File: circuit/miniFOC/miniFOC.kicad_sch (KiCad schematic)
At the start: 79 parts, among them J1 Conn_01x05, J2 Conn_01x03, J3 Conn_01x04, J4 Conn_01x02, J5 Conn_01x01, J6 Conn_01x01, J7 Conn_01x01, Q1 RU30J30M, Q2 RU30J30M, Q3 RU30J30M, U1 XC6206P332MR, U2 CH32V203C8T6, U3 LM321, U4 COS722MR, U5 BDR2L00, U6 BDR2L00, U7 BDR2L00, U8 JW5017S

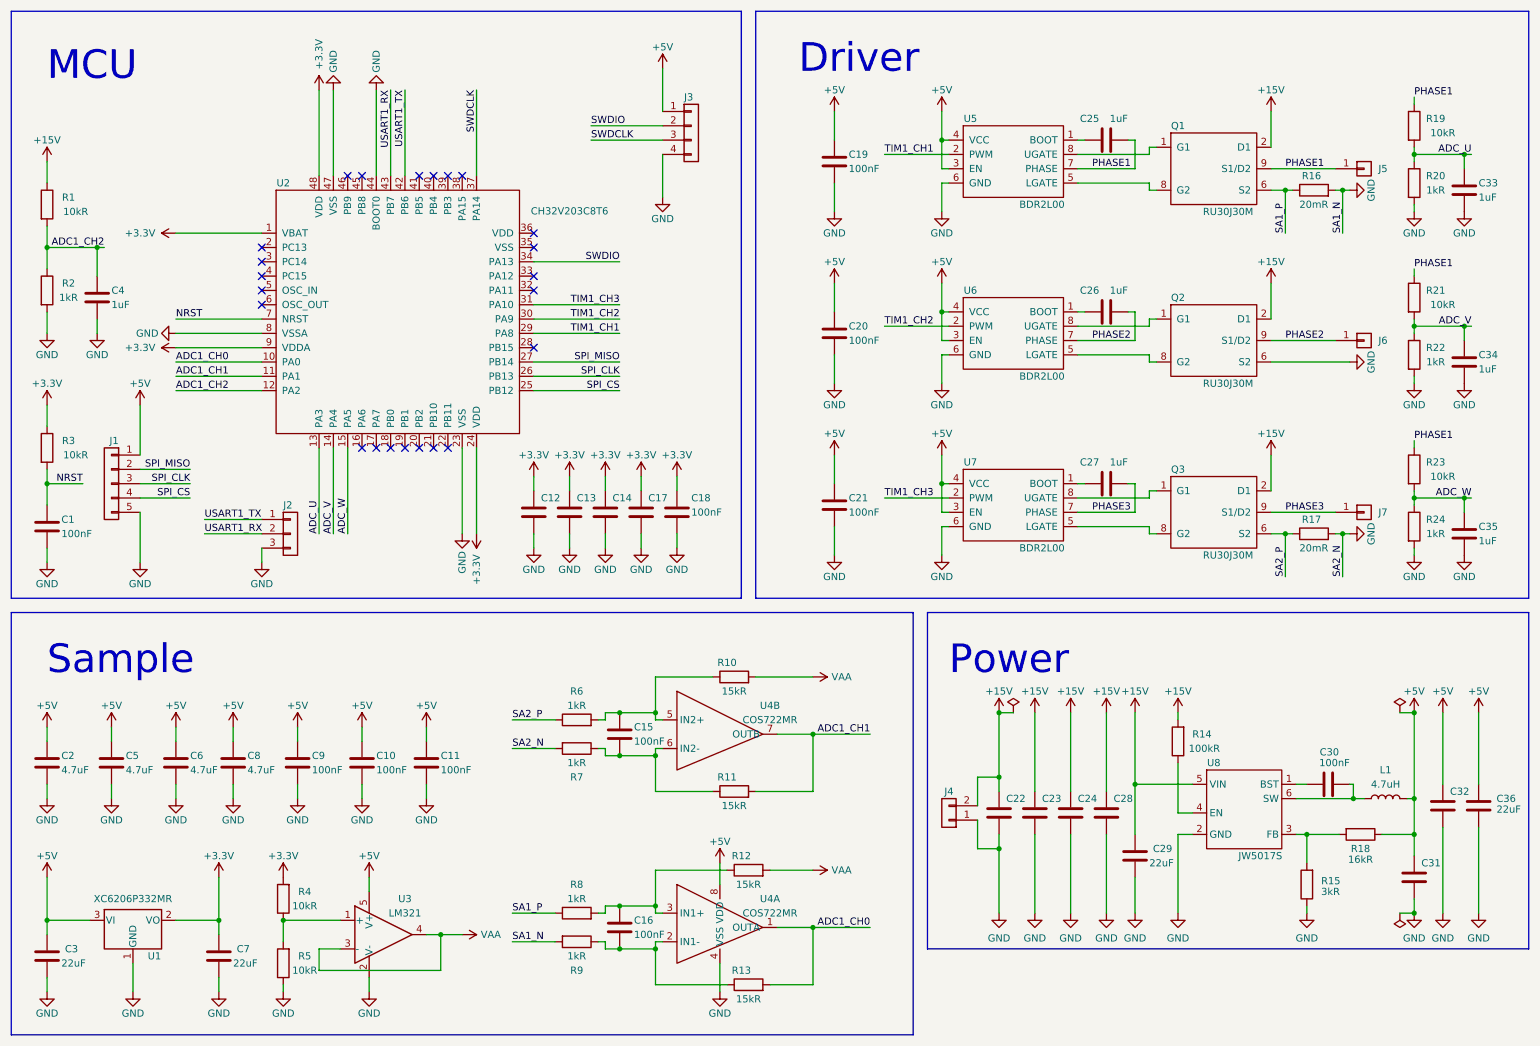
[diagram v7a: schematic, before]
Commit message: Complete the main circuit design of the second version of miniFOC and remove useless files.
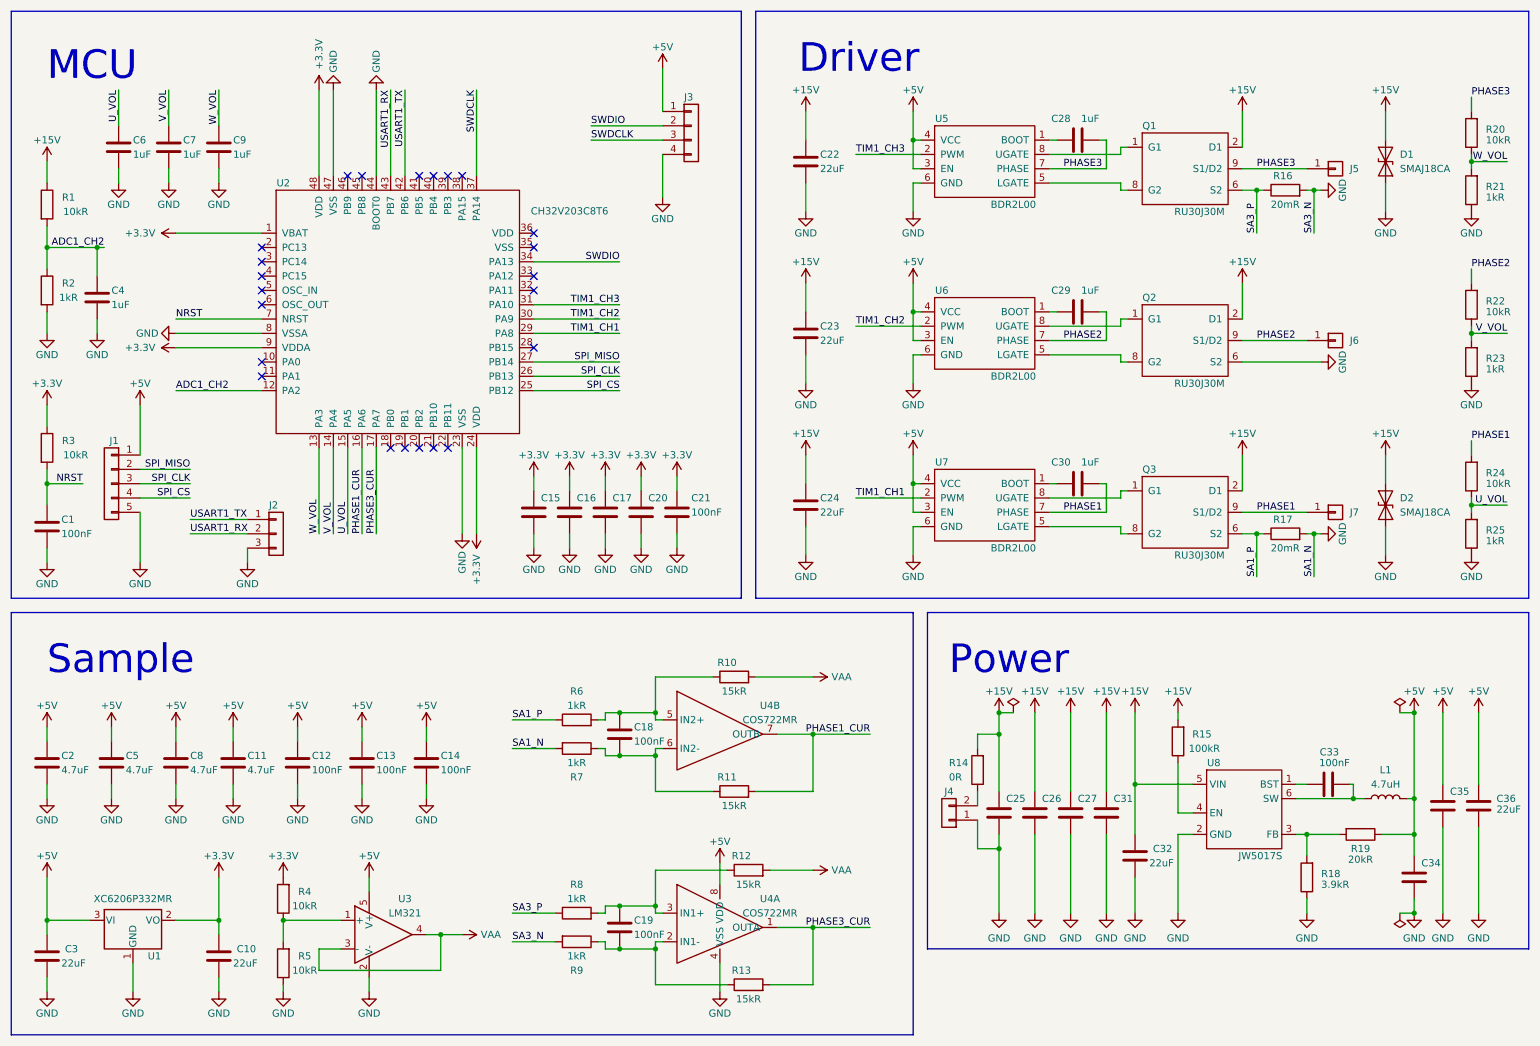
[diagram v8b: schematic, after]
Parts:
- removed C19, C20, C21: 100nF, library:C_0402_1005Metric, symbol library:C
- removed C33, C34, C35: 1uF, library:C_0402_1005Metric, symbol library:C
- removed R19: 10kR, library:R_0402_1005Metric, symbol library:R
- added C22, C23, C24: 22uF, library:C_0805_2012Metric, symbol library:C
- added C6, C7, C9: 1uF, library:C_0402_1005Metric, symbol library:C
- added D1, D2: SMAJ18CA, library:D_SMB, symbol library:SMAJ17CA
- added R14: 0R, library:R_1812_4532Metric, symbol library:R
- added R25: 1kR, library:R_0402_1005Metric, symbol library:R
- C33: renamed from C30; footprint library:C_0402_1005Metric -> library:C_1206_3216Metric
- R18: renamed from R15; value 3kR -> 3.9kR
- R19: renamed from R18; value 16kR -> 20kR
- R20, R22, R24: value 1kR -> 10kR
- R21, R23: value 10kR -> 1kR
- renumbered C7 to C10, C8 to C11, C9 to C12, C10 to C13, C11 to C14, C12 to C15, C13 to C16, C14 to C17, C15 to C18, C16 to C19, C17 to C20, C18 to C21, C22 to C25, C23 to C26, C24 to C27, C25 to C28, C26 to C29, C27 to C30, C28 to C31, C29 to C32, C31 to C34, C32 to C35, C6 to C8, R14 to R15
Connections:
- net SA2_P is gone; now on net SA1_P: Q3.5 (S2), Q3.6 (S2), Q3.7 (S2), R17.1, R6.1
- net +15V: now also C22.2, C23.2, C24.2, D1.2 (A2), D2.2 (A2), R14.2; no longer J4.2 (Pin_2)
- net EP: now also R21.1, R23.1, C22.1, C23.1, C24.1, C6.2, C7.2, C9.2, D1.1 (A1), D2.1 (A1), R25.1; no longer R20.2, R22.2, R24.2
- net PHASE1: now also C30.2, J7.1 (Pin_1), Q3.9 (S1/D2), R24.2, U7.7 (PHASE); no longer C28.2, J5.1 (Pin_1), Q1.9 (S1/D2), R21.1, R23.1, U5.7 (PHASE)
- net PHASE2: now also R22.2
- net PHASE3: now also C28.2, J5.1 (Pin_1), Q1.9 (S1/D2), R20.2, U5.7 (PHASE); no longer C30.2, J7.1 (Pin_1), Q3.9 (S1/D2), U7.7 (PHASE)
- net SA1_P: no longer Q1.5 (S2), Q1.6 (S2), Q1.7 (S2), R16.1, R8.1
- net TIM1_CH1: now also U7.2 (PWM); no longer U5.2 (PWM)
- net TIM1_CH3: now also U5.2 (PWM); no longer U7.2 (PWM)
- net PHASE1_CUR: now reaches U2.16 (PA6)
- net PHASE1_CUR: now also R11.2, U4.7 (OUTB)
- net PHASE3_CUR: now reaches U2.17 (PA7)
- net PHASE3_CUR: now also R13.2, U4.1 (OUTA)
- removed net ADC1_CH0: R13.2, U2.10 (PA0), U4.1 (OUTA)
- removed net ADC1_CH1: R11.2, U2.11 (PA1), U4.7 (OUTB)
- net ADC_U renamed W_VOL
- net W_VOL: now also R21.2, C9.1
- net ADC_V renamed V_VOL
- net V_VOL: now also R23.2, C7.1; no longer R21.2
- net ADC_W renamed U_VOL
- net U_VOL: now also C6.1, R25.2; no longer R23.2
- new net: J4.2 (Pin_2), R14.1
- new net SA3_P: Q1.5 (S2), Q1.6 (S2), Q1.7 (S2), R16.1, R8.1
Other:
- moved on the sheet: C28, C29, C30, J2, J5, J6, J7, Q1, Q2, Q3, R16, R17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
